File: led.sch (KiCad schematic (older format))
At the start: 46 parts, among them IC1 IS31FL3733-TQLS4

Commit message: first manufactured version, testing needed
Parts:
- removed D12, D15, D17, D19, D20, D22: SK6805, LED_SMD:LED_SK6812MINI_PLCC4_3.5x3.5mm_P1.75mm, symbol LED:SK6805
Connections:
- net UGLOW_LED: now also D13.3 (DIN)
- net at D14.1 (DOUT): now also D16.3 (DIN)
- net at D16.1 (DOUT): now also D18.3 (DIN)
- net at D18.1 (DOUT): now also D21.3 (DIN)
- net at D21.1 (DOUT): now also D23.3 (DIN)
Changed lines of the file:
@@
 NoConn ~ 9800 4650
-$Comp
-L LED:SK6805 D12
-U 1 1 5C2D0E89
-P 1450 6050
-F 0 "D12" H 1791 6096 50  0000 L CNN
-F 1 "SK6805" H 1791 6005 50  0000 L CNN
-F 2 "LED_SMD:LED_SK6812MINI_PLCC4_3.5x3.5mm_P1.75mm" H 1500 5750 50  0001 L TNN
-F 3 "https://cdn-shop.adafruit.com/product-files/3484/3484_Datasheet.pdf" H 1550 5675 50  0001 L TNN
-	1    1450 6050
-	1    0    0    -1
-$EndComp
 $Comp
 L LED:SK6805 D13
@@
 $EndComp
 $Comp
-L LED:SK6805 D15
-U 1 1 5C2D123C
-P 3850 5600
-F 0 "D15" H 4191 5646 50  0000 L CNN
-F 1 "SK6805" H 4191 5555 50  0000 L CNN
-F 2 "LED_SMD:LED_SK6812MINI_PLCC4_3.5x3.5mm_P1.75mm" H 3900 5300 50  0001 L TNN
-F 3 "https://cdn-shop.adafruit.com/product-files/3484/3484_Datasheet.pdf" H 3950 5225 50  0001 L TNN
-	1    3850 5600
-	1    0    0    -1
-$EndComp
-$Comp
 L LED:SK6805 D16
 U 1 1 5C2D1243
@@
 $EndComp
 $Comp
-L LED:SK6805 D17
-U 1 1 5C2D124A
-P 5300 5600
-F 0 "D17" H 5641 5646 50  0000 L CNN
-F 1 "SK6805" H 5641 5555 50  0000 L CNN
-F 2 "LED_SMD:LED_SK6812MINI_PLCC4_3.5x3.5mm_P1.75mm" H 5350 5300 50  0001 L TNN
-F 3 "https://cdn-shop.adafruit.com/product-files/3484/3484_Datasheet.pdf" H 5400 5225 50  0001 L TNN
-	1    5300 5600
-	1    0    0    -1
-$EndComp
-$Comp
 L LED:SK6805 D18
 U 1 1 5C3202D5
@@
 $EndComp
 $Comp
-L LED:SK6805 D19
-U 1 1 5C3202DC
-P 6650 5600
-F 0 "D19" H 6991 5646 50  0000 L CNN
-F 1 "SK6805" H 6991 5555 50  0000 L CNN
-F 2 "LED_SMD:LED_SK6812MINI_PLCC4_3.5x3.5mm_P1.75mm" H 6700 5300 50  0001 L TNN
-F 3 "https://cdn-shop.adafruit.com/product-files/3484/3484_Datasheet.pdf" H 6750 5225 50  0001 L TNN
-	1    6650 5600
-	1    0    0    -1
-$EndComp
-$Comp
-L LED:SK6805 D20
-U 1 1 5C3202E3
-P 7250 6050
-F 0 "D20" H 7591 6096 50  0000 L CNN
-F 1 "SK6805" H 7591 6005 50  0000 L CNN
-F 2 "LED_SMD:LED_SK6812MINI_PLCC4_3.5x3.5mm_P1.75mm" H 7300 5750 50  0001 L TNN
-F 3 "https://cdn-shop.adafruit.com/product-files/3484/3484_Datasheet.pdf" H 7350 5675 50  0001 L TNN
-	1    7250 6050
-	1    0    0    -1
-$EndComp
-$Comp
 L LED:SK6805 D21
 U 1 1 5C3202EA
@@
 $EndComp
 $Comp
-L LED:SK6805 D22
-U 1 1 5C3202F1
-P 8450 6050
-F 0 "D22" H 8791 6096 50  0000 L CNN
-F 1 "SK6805" H 8791 6005 50  0000 L CNN
-F 2 "LED_SMD:LED_SK6812MINI_PLCC4_3.5x3.5mm_P1.75mm" H 8500 5750 50  0001 L TNN
-F 3 "https://cdn-shop.adafruit.com/product-files/3484/3484_Datasheet.pdf" H 8550 5675 50  0001 L TNN
-	1    8450 6050
-	1    0    0    -1
-$EndComp
-$Comp
 L LED:SK6805 D23
 U 1 1 5C3202F8
@@
 $EndComp
 Wire Wire Line
-	1750 6050 1800 6050
-Wire Wire Line
-	1800 6050 1800 5600
-Wire Wire Line
-	1800 5600 2000 5600
-Wire Wire Line
 	2600 5600 2700 5600
 Wire Wire Line
@@
 	2700 6050 2800 6050
 Wire Wire Line
-	3400 6050 3500 6050
-Wire Wire Line
-	3500 6050 3500 5600
-Wire Wire Line
-	3500 5600 3550 5600
-Wire Wire Line
-	4150 5600 4250 5600
-Wire Wire Line
-	4250 5600 4250 6050
-Wire Wire Line
-	4250 6050 4350 6050
-Wire Wire Line
-	4950 6050 4950 5600
-Wire Wire Line
-	4950 5600 5000 5600
-Wire Wire Line
-	5600 5600 5650 5600
-Wire Wire Line
-	5650 5600 5650 6050
-Wire Wire Line
-	5650 6050 5700 6050
-Wire Wire Line
-	6300 6050 6300 5600
-Wire Wire Line
-	6300 5600 6350 5600
-Wire Wire Line
-	6950 5600 6950 6050
-Wire Wire Line
-	7550 6050 7550 5600
-Wire Wire Line
-	8150 5600 8150 6050
-Wire Wire Line
 	2300 5300 3100 5300
-Wire Wire Line
-	5300 5300 6000 5300
-Wire Wire Line
-	7850 5300 7250 5300
-Connection ~ 6650 5300
-Wire Wire Line
-	7850 5300 8450 5300
 Connection ~ 7850 5300
-Wire Wire Line
-	3850 5300 4650 5300
-Connection ~ 3850 5300
-Connection ~ 5300 5300
-Wire Wire Line
-	1450 6350 2300 6350
-Wire Wire Line
-	3100 6350 3850 6350
 Connection ~ 3100 6350
-Wire Wire Line
-	4650 6350 5300 6350
 Connection ~ 4650 6350
-Wire Wire Line
-	6000 6350 6650 6350
 Connection ~ 6000 6350
-Wire Wire Line
-	7250 6350 7850 6350
-Connection ~ 7250 6350
 $Comp
 L power:GND #PWR0131
@@
 	0    1    1    0
 $EndComp
-Wire Wire Line
-	1050 5300 1450 5300
 Connection ~ 2300 5300
-Wire Wire Line
-	1050 6350 1450 6350
-Connection ~ 1450 6350
 Text HLabel 1050 6050 0    50   Input ~ 0
 UGLOW_LED
 Wire Wire Line
-	1050 6050 1150 6050
-Wire Wire Line
-	8750 6050 8750 5600
-Wire Wire Line
-	8750 5600 8800 5600
-Wire Wire Line
-	7250 5750 7250 5300
-Connection ~ 7250 5300
-Wire Wire Line
-	7250 5300 6650 5300
-Wire Wire Line
-	8450 5750 8450 5300
-Connection ~ 8450 5300
-Wire Wire Line
-	8450 5300 9100 5300
-Wire Wire Line
 	6000 5750 6000 5300
 Connection ~ 6000 5300
 Wire Wire Line
-	6000 5300 6650 5300
-Wire Wire Line
 	4650 5750 4650 5300
 Connection ~ 4650 5300
 Wire Wire Line
-	4650 5300 5300 5300
-Wire Wire Line
 	3100 5750 3100 5300
 Connection ~ 3100 5300
 Wire Wire Line
-	3100 5300 3850 5300
-Wire Wire Line
-	1450 5750 1450 5300
-Connection ~ 1450 5300
-Wire Wire Line
-	1450 5300 2300 5300
-Wire Wire Line
 	2300 5900 2300 6350
 Connection ~ 2300 6350
@@
 	2300 6350 3100 6350
 Wire Wire Line
-	3850 5900 3850 6350
-Connection ~ 3850 6350
-Wire Wire Line
-	3850 6350 4650 6350
-Wire Wire Line
-	5300 5900 5300 6350
-Connection ~ 5300 6350
-Wire Wire Line
-	5300 6350 6000 6350
-Wire Wire Line
-	6650 5900 6650 6350
-Connection ~ 6650 6350
-Wire Wire Line
-	6650 6350 7250 6350
-Wire Wire Line
 	7850 5900 7850 6350
 Connection ~ 7850 6350
 Wire Wire Line
-	7850 6350 8450 6350
-Wire Wire Line
-	8450 6350 9100 6350
-Wire Wire Line
 	9100 6350 9100 5900
-Connection ~ 8450 6350
 $Comp
 L Device:C C18
@@
 	0    -1   -1   0
 $EndComp
+Wire Wire Line
+	4650 5300 6000 5300
+Wire Wire Line
+	7850 6350 9100 6350
+Wire Wire Line
+	4650 6350 6000 6350
+Wire Wire Line
+	7850 5300 9100 5300
+Wire Wire Line
+	3100 5300 4650 5300
+Wire Wire Line
+	1050 6350 2300 6350
+Wire Wire Line
+	6000 5300 7850 5300
+Wire Wire Line
+	6000 6350 7850 6350
+Wire Wire Line
+	3100 6350 4650 6350
+Wire Wire Line
+	1050 5300 2300 5300
+Wire Wire Line
+	1550 6050 1550 5600
+Wire Wire Line
+	1550 5600 2000 5600
+Wire Wire Line
+	1050 6050 1550 6050
+Wire Wire Line
+	3400 6050 4350 6050
+Wire Wire Line
+	4950 6050 5700 6050
+Wire Wire Line
+	6300 6050 7200 6050
+Wire Wire Line
+	7200 6050 7200 5600
+Wire Wire Line
+	7200 5600 7550 5600
+Wire Wire Line
+	8150 5600 8800 5600
 $EndSCHEMATC

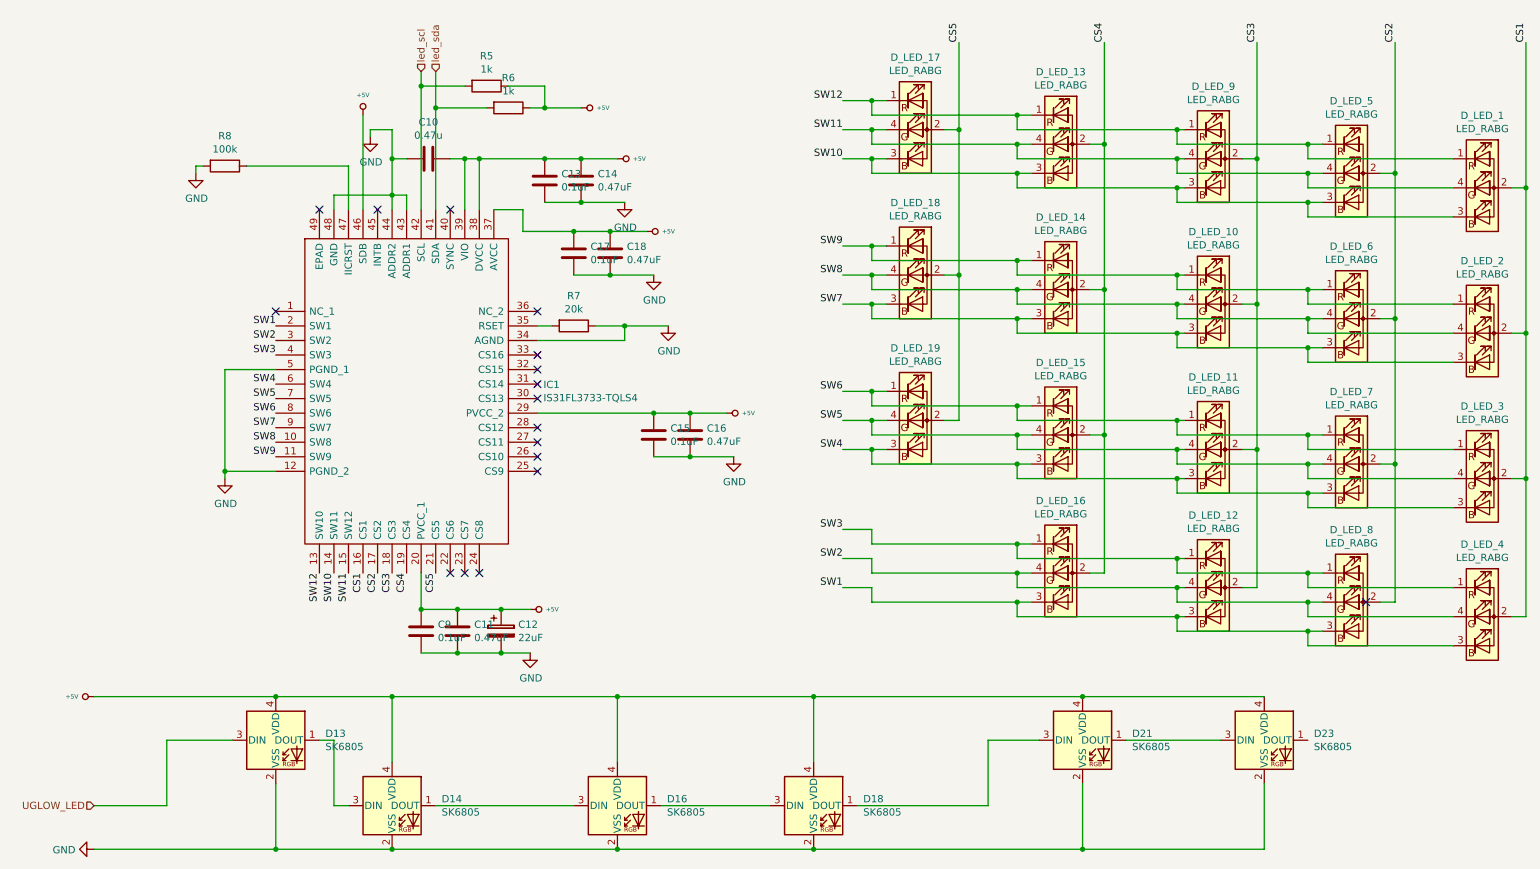
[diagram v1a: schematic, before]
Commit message: Auf STM32F303 Controller umgestiegen. RGB per Switch rausgeflogen.
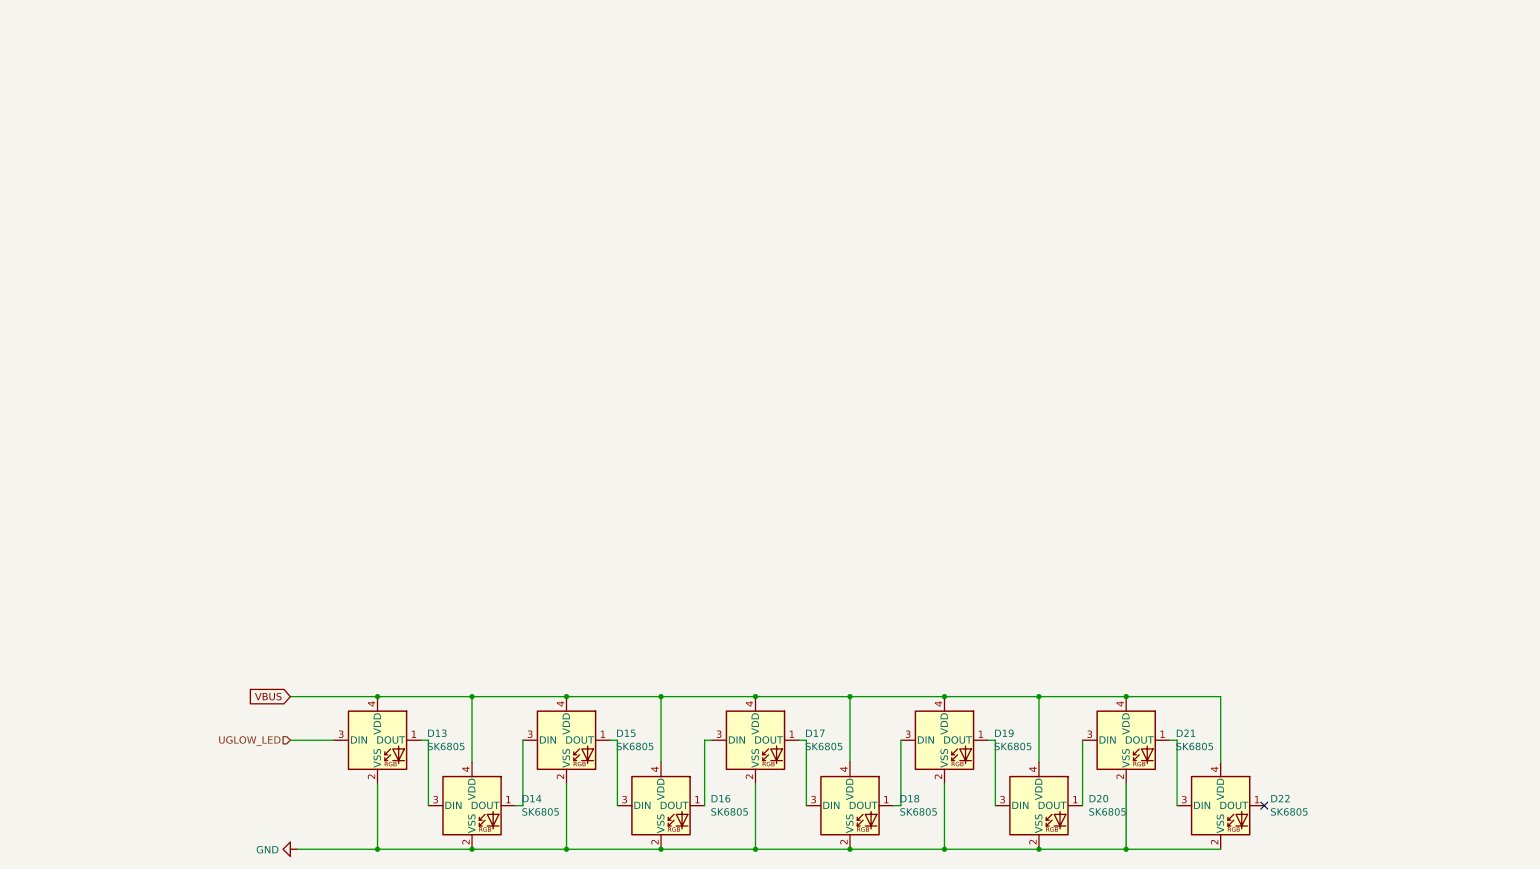
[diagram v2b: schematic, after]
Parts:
- removed C10: 0.47u, Capacitor_SMD:C_0805_2012Metric_Pad1.15x1.40mm_HandSolder, symbol Device:C
- removed C11, C14, C16, C18: 0.47uF, Capacitor_SMD:C_0805_2012Metric_Pad1.15x1.40mm_HandSolder, symbol Device:C
- removed C12: 22uF, Capacitor_SMD:C_0805_2012Metric_Pad1.15x1.40mm_HandSolder, symbol Device:CP
- removed C13, C15, C17, C9: 0.1uF, Capacitor_SMD:C_0805_2012Metric_Pad1.15x1.40mm_HandSolder, symbol Device:C
- removed D_LED_1, D_LED_10, D_LED_11, D_LED_12, D_LED_13, D_LED_14, D_LED_15, D_LED_16, D_LED_17, D_LED_18, D_LED_19, D_LED_2, D_LED_3, D_LED_4, D_LED_5, D_LED_6, D_LED_7, D_LED_8, D_LED_9: LED_RABG, reverse_RGB_LED:reverse_RGB_LED, symbol Device:LED_RABG
- removed IC1: IS31FL3733-TQLS4, Package_DFN_QFN:QFN-48-1EP_6x6mm_P0.4mm_EP4.3x4.3mm, symbol IS31FL3733-TQLS4:IS31FL3733-TQLS4
- removed R5, R6: 1k, Resistor_SMD:R_0805_2012Metric_Pad1.15x1.40mm_HandSolder, symbol Device:R
- removed R7: 20k, Resistor_SMD:R_0805_2012Metric_Pad1.15x1.40mm_HandSolder, symbol Device:R
- removed R8: 100k, Resistor_SMD:R_0805_2012Metric_Pad1.15x1.40mm_HandSolder, symbol Device:R
- added D15, D17, D19, D21: SK6805, LED_SMD:LED_SK6812MINI_PLCC4_3.5x3.5mm_P1.75mm, symbol LED:SK6805
- renumbered D21 to D20, D23 to D22
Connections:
- net GND: now also D15.2 (VSS), D17.2 (VSS), D19.2 (VSS), D21.2 (VSS)
- net at D14.1 (DOUT): now also D15.3 (DIN); no longer D16.3 (DIN)
- net at D16.1 (DOUT): now also D17.3 (DIN); no longer D18.3 (DIN)
- net at D18.1 (DOUT): now also D19.3 (DIN); no longer D20.3 (DIN)
- net at D20.1 (DOUT): now also D21.3 (DIN); no longer D22.3 (DIN)
- net +5V renamed VBUS
- net VBUS: now also D15.4 (VDD), D17.4 (VDD), D19.4 (VDD), D21.4 (VDD)
- new net: D15.1 (DOUT), D16.3 (DIN)
- new net: D17.1 (DOUT), D18.3 (DIN)
- new net: D19.1 (DOUT), D20.3 (DIN)
- new net: D21.1 (DOUT), D22.3 (DIN)
- no-connect marks 17 -> 1
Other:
- moved on the sheet: D13, D14, D16, D18, D20, D22
